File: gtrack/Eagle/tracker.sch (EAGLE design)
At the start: 59 parts, among them IC1 STM32L152RBT, IC2 TPS73601, U2 SIM900, U3 MCP73831, X1 MINI-USB-32005-301

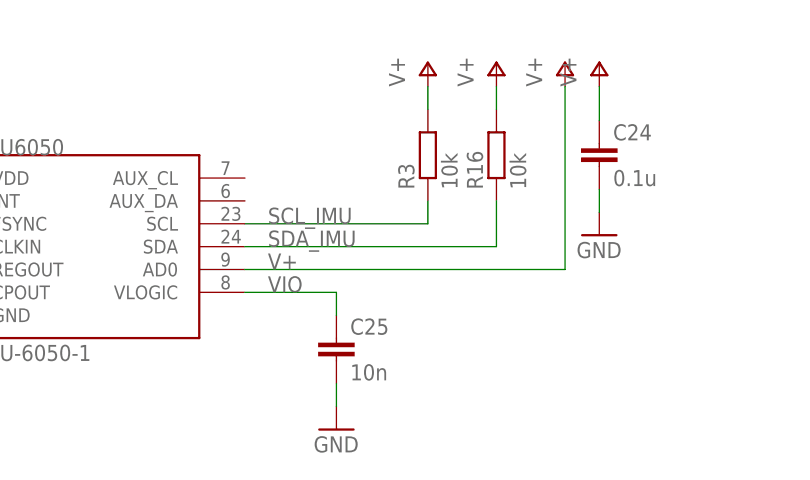
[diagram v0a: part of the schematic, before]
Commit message: Fixed issue with missing MPU6050 power trace
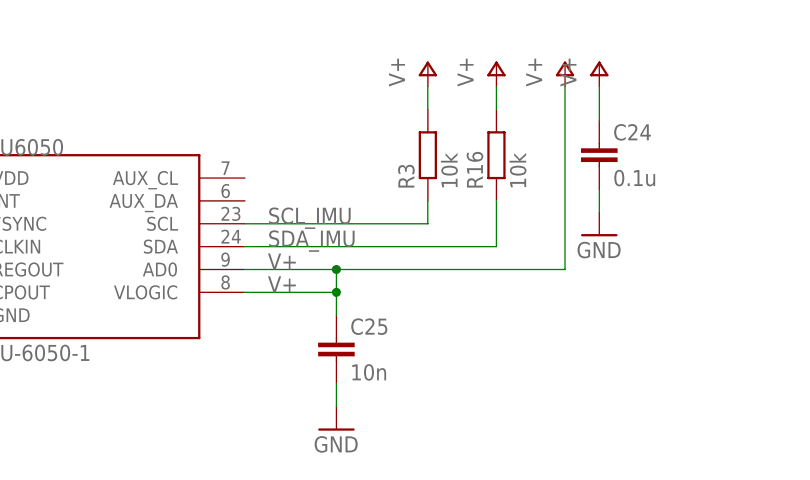
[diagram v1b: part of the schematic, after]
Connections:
- removed net VIO: C25.1, MPU6050.VLOGIC
- net V+: now also C25.1, MPU6050.VLOGIC
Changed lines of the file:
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@@
 <setting verticaltext="up"/>
 </settings>
-<grid distance="0.1" unitdist="inch" unit="inch" style="lines" multiple="1" display="no" altdistance="0.01" altunitdist="inch" altunit="inch"/>
+<grid distance="0.01" unitdist="inch" unit="inch" style="lines" multiple="1" display="yes" altdistance="0.01" altunitdist="inch" altunit="inch"/>
 <layers>
 <layer number="1" name="Top" color="4" fill="1" visible="no" active="no"/>
@@
 </segment>
 </net>
-<net name="VIO" class="0">
-<segment>
-<wire x1="-13.97" y1="-80.01" x2="-3.81" y2="-80.01" width="0.1524" layer="91"/>
-<pinref part="MPU6050" gate="G$1" pin="VLOGIC"/>
-<pinref part="C25" gate="G$1" pin="1"/>
-<wire x1="-3.81" y1="-82.55" x2="-3.81" y2="-80.01" width="0.1524" layer="91"/>
-<label x="-11.43" y="-80.01" size="1.778" layer="95"/>
-</segment>
-</net>
 <net name="VCC_GSM" class="0">
 <segment>
@@
 <label x="-11.43" y="-77.47" size="1.778" layer="95"/>
 <pinref part="MPU6050" gate="G$1" pin="AD0"/>
-<wire x1="-13.97" y1="-77.47" x2="21.59" y2="-77.47" width="0.1524" layer="91"/>
+<wire x1="-13.97" y1="-77.47" x2="-3.81" y2="-77.47" width="0.1524" layer="91"/>
 <pinref part="P+4" gate="1" pin="V+"/>
-</segment>
-<segment>
+<wire x1="-3.81" y1="-77.47" x2="21.59" y2="-77.47" width="0.1524" layer="91"/>
+<wire x1="-13.97" y1="-80.01" x2="-3.81" y2="-80.01" width="0.1524" layer="91"/>
+<pinref part="MPU6050" gate="G$1" pin="VLOGIC"/>
+<pinref part="C25" gate="G$1" pin="1"/>
+<wire x1="-3.81" y1="-82.55" x2="-3.81" y2="-80.01" width="0.1524" layer="91"/>
+<label x="-11.43" y="-80.01" size="1.778" layer="95"/>
+<wire x1="-3.81" y1="-80.01" x2="-3.81" y2="-77.47" width="0.1524" layer="91"/>
+<junction x="-3.81" y="-80.01"/>
+<junction x="-3.81" y="-77.47"/>
+</segment>
+<segment>

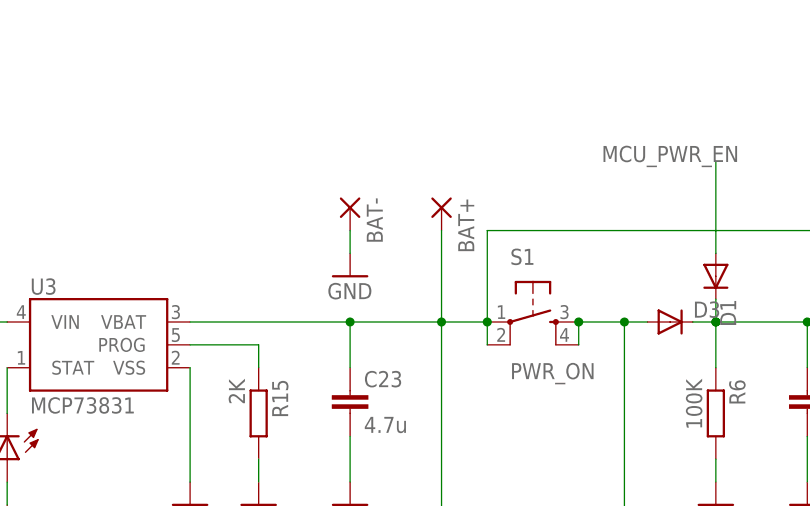
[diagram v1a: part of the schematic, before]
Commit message: Add battery connector to PCB
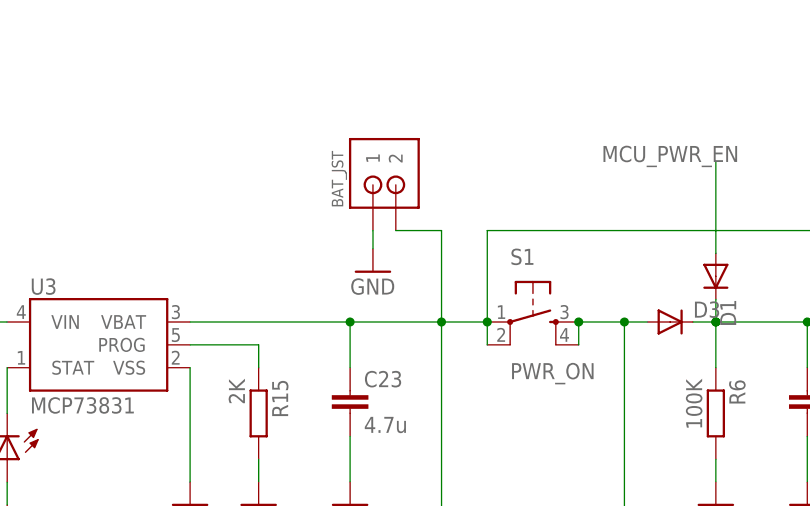
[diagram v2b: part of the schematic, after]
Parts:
- removed BAT+, BAT-: (no value), wirepad:SMD2
- added BAT_JST: JST-PH_2-PIN_HEADER, SRG:JST-PH_2-PIN_HEADER
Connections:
- net GND: now also BAT_JST.1; no longer BAT-.P
- net GSM_VBAT: now also BAT_JST.2; no longer BAT+.P
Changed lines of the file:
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@@
 <attribute name="OC_NEWARK" value="unknown"/>
 </part>
-<part name="BAT+" library="wirepad" deviceset="SMD2" device=""/>
-<part name="BAT-" library="wirepad" deviceset="SMD2" device=""/>
 <part name="GND1" library="SparkFun" deviceset="GND" device=""/>
 <part name="GSM_PWR" library="mmun221X" deviceset="MMUN221X" device=""/>
@@
 <part name="P+7" library="supply1" deviceset="V+" device=""/>
 <part name="P+6" library="supply1" deviceset="V+" device=""/>
+<part name="BAT_JST" library="SRG" deviceset="JST-PH_2-PIN_HEADER" device=""/>
 </parts>
 <sheets>
@@
 <attribute name="MPN" x="121.92" y="88.9" size="1.778" layer="96" display="off"/>
 </instance>
-<instance part="BAT+" gate="1" x="-116.84" y="109.22" rot="R270"/>
-<instance part="BAT-" gate="1" x="-127" y="109.22" rot="R270"/>
-<instance part="GND1" gate="1" x="-127" y="101.6"/>
+<instance part="GND1" gate="1" x="-124.46" y="102.108"/>
 <instance part="GSM_PWR" gate="G$1" x="-160.02" y="-73.66"/>
 <instance part="GSM_RST" gate="G$1" x="-106.68" y="-73.66"/>
@@
 <instance part="P+7" gate="1" x="135.89" y="127"/>
 <instance part="P+6" gate="1" x="-7.62" y="110.49"/>
+<instance part="BAT_JST" gate="G$1" x="-121.92" y="114.3" smashed="yes" rot="R90">
+<attribute name="NAME" x="-127.762" y="109.22" size="1.27" layer="95" font="vector" rot="R90"/>
+</instance>
 </instances>
 <busses>
@@
 </segment>
 <segment>
-<pinref part="BAT-" gate="1" pin="P"/>
-<pinref part="GND1" gate="1" pin="GND"/>
-<wire x1="-127" y1="106.68" x2="-127" y2="104.14" width="0.1524" layer="91"/>
-</segment>
-<segment>
 <pinref part="GSM_RST" gate="G$1" pin="E"/>
 <pinref part="GND7" gate="1" pin="GND"/>
@@
 <pinref part="GSM_PWR" gate="G$1" pin="E"/>
 <wire x1="-154.94" y1="-86.36" x2="-154.94" y2="-83.82" width="0.1524" layer="91"/>
+</segment>
+<segment>
+<pinref part="BAT_JST" gate="G$1" pin="1"/>
+<pinref part="GND1" gate="1" pin="GND"/>
+<wire x1="-124.46" y1="106.68" x2="-124.46" y2="104.648" width="0.1524" layer="91"/>
 </segment>
 </net>
@@
 <wire x1="-63.5" y1="91.44" x2="-63.5" y2="106.68" width="0.1524" layer="91"/>
 <junction x="-63.5" y="106.68"/>
-<pinref part="BAT+" gate="1" pin="P"/>
 <wire x1="-116.84" y1="96.52" x2="-116.84" y2="106.68" width="0.1524" layer="91"/>
-</segment>
-<segment>
+<pinref part="BAT_JST" gate="G$1" pin="2"/>
+<wire x1="-116.84" y1="106.68" x2="-121.92" y2="106.68" width="0.1524" layer="91"/>
+</segment>
+<segment>
